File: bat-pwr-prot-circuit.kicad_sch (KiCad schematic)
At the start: 14 parts, among them IC1 FS312F-G, IC2 3v3 Regulator, J1 Bat+, J2 3v3, J3 Battery, J4 Bat+, J5 3v3, J6 Chg, Q1 FS8205

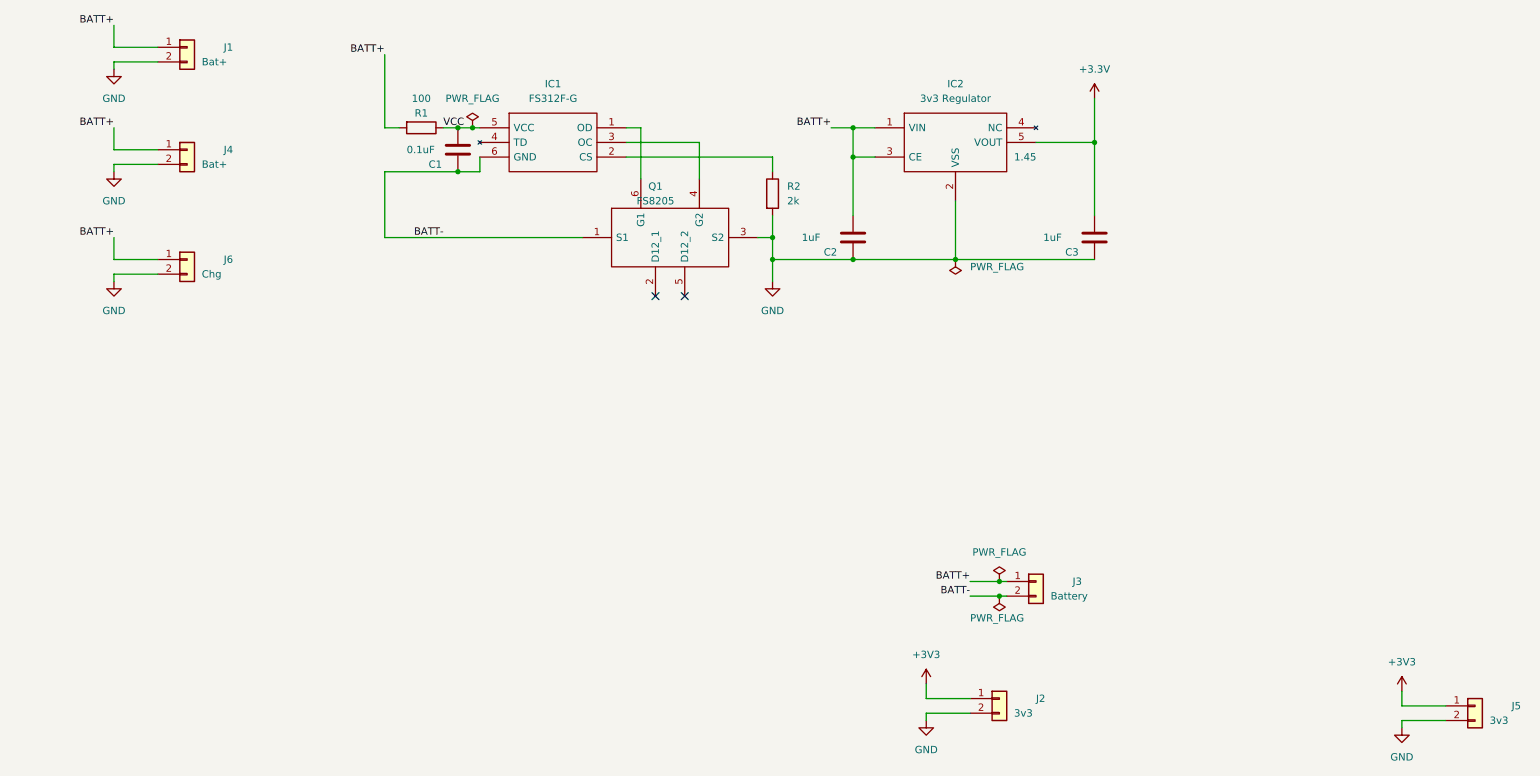
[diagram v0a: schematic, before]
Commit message: Selectable rails and led indicators
- Added pin selectory to configure the left and right rail connectors individually for batt+ and 3v3
- Added led indicators for batt+ and 3v3
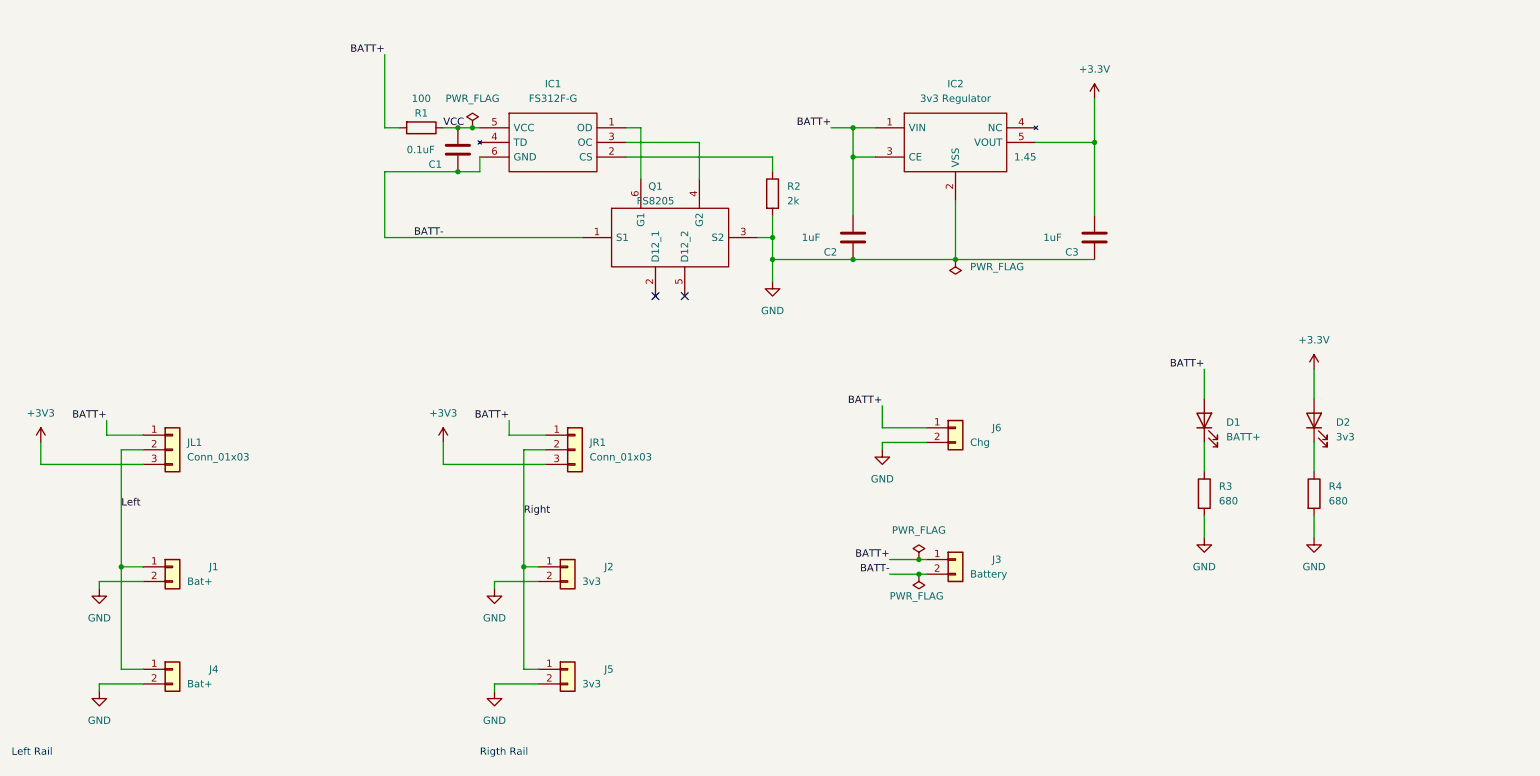
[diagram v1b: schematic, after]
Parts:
- added D1: BATT+, LED_SMD:LED_0201_0603Metric_Pad0.64x0.40mm_HandSolder, symbol Device:LED
- added D2: 3v3, symbol Device:LED
- added JL1, JR1: Conn_01x03, Connector_PinHeader_2.54mm:PinHeader_1x03_P2.54mm_Vertical, symbol Connector_Generic:Conn_01x03
- added R3: 680, Resistor_SMD:R_0603_1608Metric_Pad0.98x0.95mm_HandSolder, symbol Device:R
- added R4: 680, symbol Device:R
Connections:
- net +3V3: now also D2.2 (A), JL1.3 (Pin_3), JR1.3 (Pin_3); no longer J2.1 (Pin_1), J5.1 (Pin_1)
- net BATT+: now also D1.2 (A), JL1.1 (Pin_1), JR1.1 (Pin_1); no longer J1.1 (Pin_1), J4.1 (Pin_1)
- net GND: now also R3.2, R4.2
- new net: D1.1 (K), R3.1
- new net: D2.1 (K), R4.1
- new net Left: J1.1 (Pin_1), J4.1 (Pin_1), JL1.2 (Pin_2)
- new net Right: J2.1 (Pin_1), J5.1 (Pin_1), JR1.2 (Pin_2)
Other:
- note added: "Left Rail"
- note added: "Rigth Rail"
- moved on the sheet: J1, J2, J3, J4, J5, J6

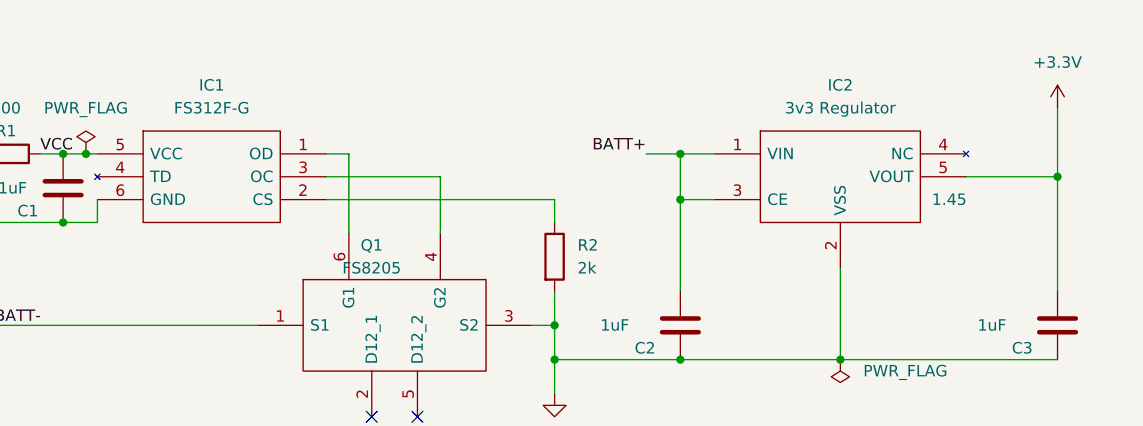
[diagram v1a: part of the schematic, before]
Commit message: Updated template for KiCAD 7
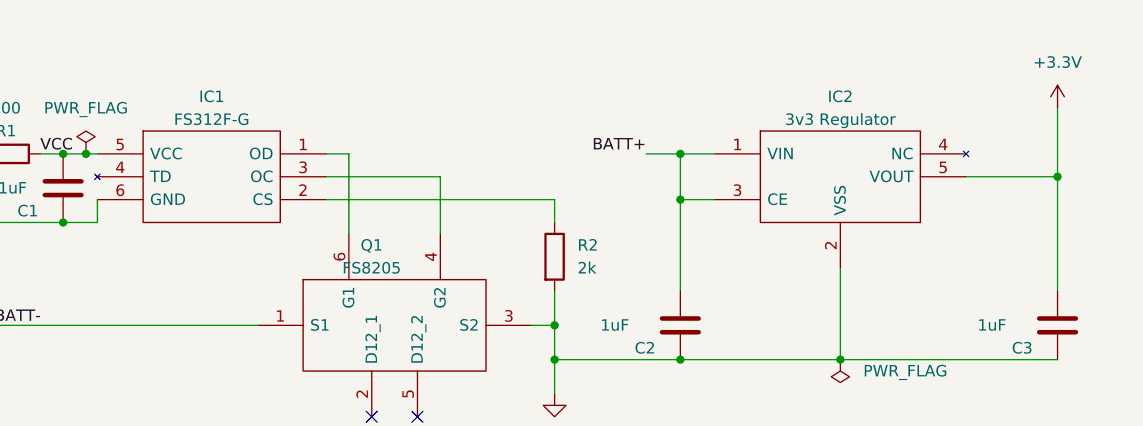
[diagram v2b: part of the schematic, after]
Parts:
- D2: footprint (none) -> LED_SMD:LED_0201_0603Metric_Pad0.64x0.40mm_HandSolder
- IC1: footprint footprints:SOT95P280X145-6N -> SOT95P280X145-6N; symbol Li-Ion Charging:FS312F-G -> Chof747 Battery Management:FS312F-G
- IC2: footprint footprints:SOT95P270X145-5N -> SOT95P270X145-5N; symbol Regulator_Linear:ME6211C33M5G-N -> Chof747 Voltage Regulators:ME6211C33M5G-N
- Q1: footprint footprints:FS8205 -> FS8205; symbol FS8205:FS8205 -> Chof747 Transistors and Mosfets:FS8205
- R4: footprint (none) -> Resistor_SMD:R_0603_1608Metric_Pad0.98x0.95mm_HandSolder
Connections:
- net +3V3: no longer C3.1, D2.2 (A), IC2.5 (VOUT)
- new net +3.3V: C3.1, D2.2 (A), IC2.5 (VOUT)
